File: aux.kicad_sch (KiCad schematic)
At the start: 17 parts, among them J7 USB_C_Receptacle_USB2.0_16P, J86 Conn_01x02_Pin, Q81 Si2301CDS, Q82 AO3400A, U85 DAC80508xRTE

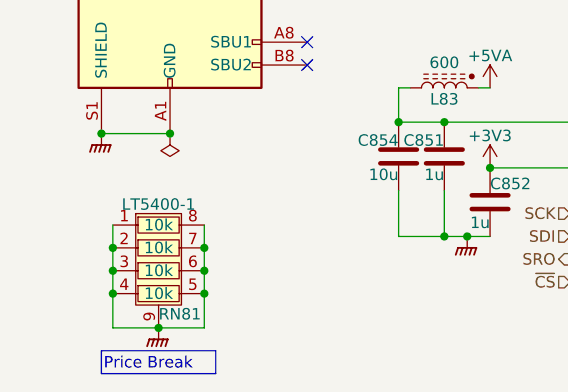
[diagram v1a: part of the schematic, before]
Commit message: Put ref filtering into the schematic.
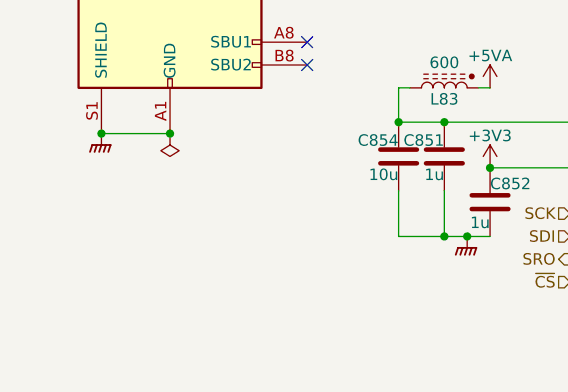
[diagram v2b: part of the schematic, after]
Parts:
- removed RN81: LT5400-1, Parts:MSOP-8-1EP_3x3mm_P0.65mm_EP1.68x1.88mm, symbol Parts:LT5400

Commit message: Progress checkin.  About to redo FDA feedback again.
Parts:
- renumbered R851 to R87, R852 to R88, R854 to R89
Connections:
- net GNDPWR: now also R89.2; no longer R89.1
- net PWR_EN: now also R89.1; no longer R89.2
- net VDAC: now reaches C851.1, C854.1, L83.2, U85.7 (VDD)
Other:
- moved on the sheet: C851, C852, C854, L83, U85

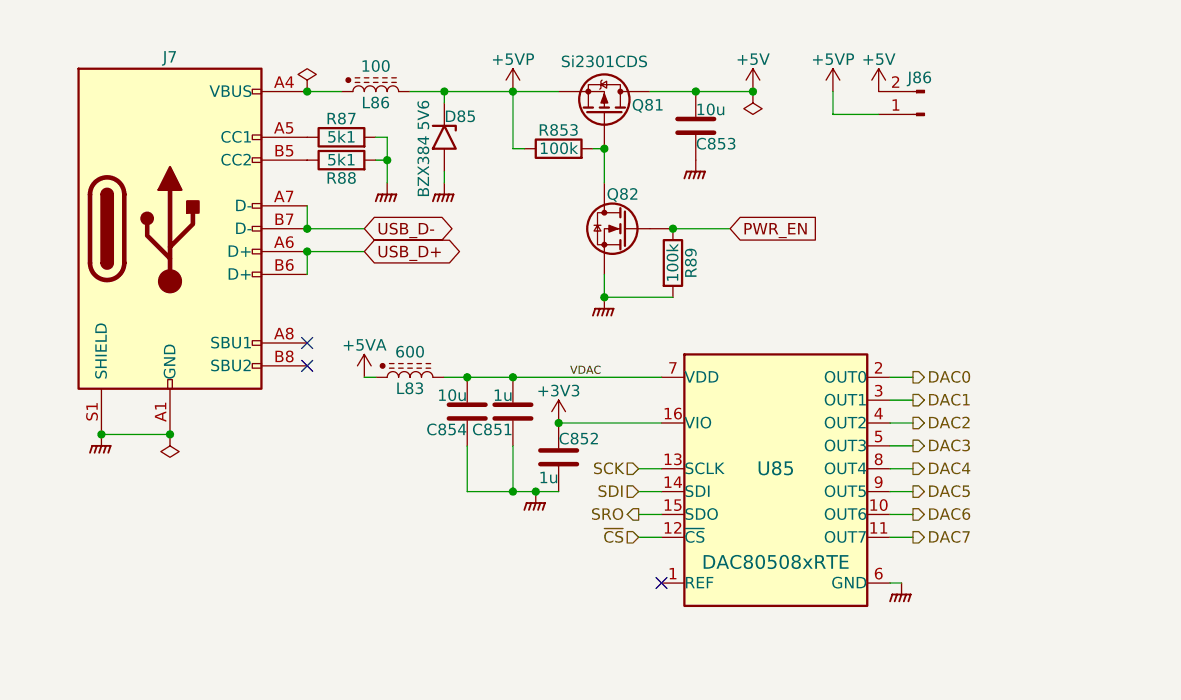
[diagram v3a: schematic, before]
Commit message: Start to place within physical board size.
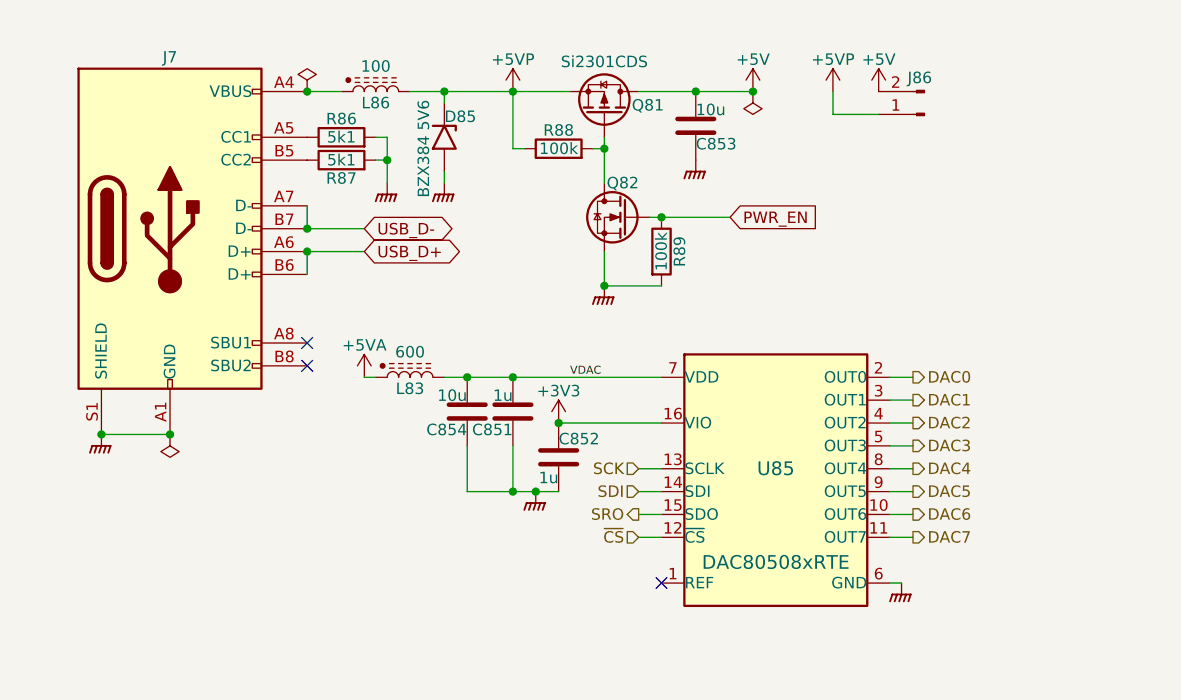
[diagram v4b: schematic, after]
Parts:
- Q81: symbol External:Si2301CDS -> Parts:Si2301CDS
- Q82: symbol Transistor_FET:AO3400A -> Parts:AO3400A; LCSC C20917 -> C15127
- renumbered R87 to R86, R88 to R87, R853 to R88
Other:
- moved on the sheet: Q81, Q82, R89
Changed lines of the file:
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@@
+	)
+	(junction
+		(at 129.54 33.02)
+		(diameter 0)
+		(color 0 0 0 0)
 	)
 	(junction
@@
 	)
 	(junction
-		(at 129.54 33.02)
-		(diameter 0)
-		(color 0 0 0 0)
-	)
-	(junction
-		(at 129.54 49.53)
+		(at 129.54 48.26)
 		(diameter 0)
 		(color 0 0 0 0)
@@
 	)
 	(junction
-		(at 137.16 41.91)
-		(diameter 0)
-		(color 0 0 0 0)
-	)
-	(junction
 		(at 119.38 71.12)
 		(diameter 0)
@@
 	)
 	(junction
+		(at 135.89 40.64)
+		(diameter 0)
+		(color 0 0 0 0)
+	)
+	(junction
 		(at 114.3 58.42)
 		(diameter 0)
@@
 	(wire
 		(pts
-			(xy 129.54 49.53) (xy 137.16 49.53)
+			(xy 129.54 48.26) (xy 135.89 48.26)
 		)
 		(stroke
@@
 	(wire
 		(pts
-			(xy 134.62 26.67) (xy 139.7 26.67)
-		)
-		(stroke
-			(width 0)
-			(type default)
-		)
-	)
-	(wire
-		(pts
 			(xy 161.29 76.2) (xy 163.83 76.2)
 		)
@@
 	(wire
 		(pts
+			(xy 129.54 31.75) (xy 129.54 33.02)
+		)
+		(stroke
+			(width 0)
+			(type default)
+		)
+	)
+	(wire
+		(pts
+			(xy 134.62 40.64) (xy 135.89 40.64)
+		)
+		(stroke
+			(width 0)
+			(type default)
+		)
+	)
+	(wire
+		(pts
 			(xy 96.52 41.91) (xy 102.87 41.91)
 		)
@@
 	(wire
 		(pts
-			(xy 129.54 46.99) (xy 129.54 49.53)
+			(xy 129.54 44.45) (xy 129.54 48.26)
 		)
 		(stroke
@@
 	(wire
 		(pts
+			(xy 133.35 26.67) (xy 139.7 26.67)
+		)
+		(stroke
+			(width 0)
+			(type default)
+		)
+	)
+	(wire
+		(pts
 			(xy 133.35 68.58) (xy 135.89 68.58)
 		)
@@
 	(wire
 		(pts
-			(xy 119.38 26.67) (xy 124.46 26.67)
+			(xy 119.38 26.67) (xy 125.73 26.67)
 		)
 		(stroke
@@
 	(wire
 		(pts
-			(xy 137.16 41.91) (xy 143.51 41.91)
+			(xy 135.89 40.64) (xy 143.51 40.64)
 		)
 		(stroke
@@
 	(global_label "PWR_EN"
 		(shape input)
-		(at 143.51 41.91 0)
+		(at 143.51 40.64 0)
 		(fields_autoplaced yes)
 		(effects
@@
 		)
 		(property "Intersheetrefs" "${INTERSHEET_REFS}"
-			(at 153.9337 41.91 0)
+			(at 153.9337 40.64 0)
 			(effects
 				(font
@@
 	)
 	(symbol
-		(lib_id "External:Si2301CDS")
+		(lib_id "Parts:Si2301CDS")
 		(at 129.54 29.21 270)
 		(mirror x)
@@
 			)
 		)
-		(property "Datasheet" "https://www.taiwansemi.com/products/datasheet/TSM2301A_C15.pdf"
+		(property "Datasheet" "~"
 			(at 125.73 24.13 0)
 			(effects
@@
 			)
 		)
-		(property "Description" "-2.8A Id, -20V Vds, P-Channel MOSFET, SOT-23"
+		(property "Description" "P-MOSFET transistor, gate/source/drain"
 			(at 129.54 29.21 0)
 			(effects
@@
 		(on_board yes)
 		(dnp no)
-		(property "Reference" "R87"
+		(property "Reference" "R86"
 			(at 100.33 29.718 90)
 			(effects
@@
 			(project "lincal"
 				(path "/b054cef4-39e3-49d8-aff0-7ba5a206c187/f6066de6-625c-453e-a76c-ce9a6a5c6264"
-					(reference "R87")
+					(reference "R86")
 					(unit 1)
 				)
@@
 		(on_board yes)
 		(dnp no)
-		(property "Reference" "R853"
+		(property "Reference" "R88"
 			(at 124.46 30.988 90)
 			(effects
@@
 			(project "lincal"
 				(path "/b054cef4-39e3-49d8-aff0-7ba5a206c187/f6066de6-625c-453e-a76c-ce9a6a5c6264"
-					(reference "R853")
+					(reference "R88")
 					(unit 1)
 				)
@@
 		(on_board yes)
 		(dnp no)
-		(property "Reference" "R88"
+		(property "Reference" "R87"
 			(at 100.33 36.322 90)
 			(effects
@@
 			(project "lincal"
 				(path "/b054cef4-39e3-49d8-aff0-7ba5a206c187/f6066de6-625c-453e-a76c-ce9a6a5c6264"
-					(reference "R88")
+					(reference "R87")
 					(unit 1)
 				)
@@
 	(symbol
 		(lib_id "power:GNDPWR")
-		(at 129.54 49.53 0)
+		(at 129.54 48.26 0)
 		(unit 1)
 		(exclude_from_sim no)
@@
 		(dnp no)
 		(property "Reference" "#PWR0104"
-			(at 129.54 55.88 0)
+			(at 129.54 54.61 0)
 			(effects
 				(font
@@
 		)
 		(property "Value" "GNDPWR"
-			(at 129.54 52.832 0)
+			(at 129.54 51.562 0)
 			(effects
 				(font
@@
 		)
 		(property "Footprint" ""
-			(at 129.54 50.8 0)
+			(at 129.54 49.53 0)
 			(effects
 				(font
@@
 		)
 		(property "Datasheet" ""
-			(at 129.54 50.8 0)
+			(at 129.54 49.53 0)
 			(effects
 				(font
@@
 		)
 		(property "Description" "Power symbol creates a global label with name \"GNDPWR\" , global ground"
-			(at 129.54 49.53 0)
+			(at 129.54 48.26 0)
 			(effects
 				(font
@@
 	)
 	(symbol
-		(lib_id "Transistor_FET:AO3400A")
-		(at 132.08 41.91 0)
+		(lib_id "Parts:AO3400A")
+		(at 132.08 40.64 0)
 		(mirror y)
 		(unit 1)
@@
 		(dnp no)
 		(property "Reference" "Q82"
-			(at 129.794 38.1 0)
+			(at 129.794 36.83 0)
 			(effects
 				(font
@@
 		)
 		(property "Value" "AO3400A"
-			(at 129.286 45.466 0)
+			(at 129.286 44.196 0)
 			(effects
 				(font
@@
 		)
 		(property "Footprint" "Parts:SOT-23"
-			(at 127 43.815 0)
+			(at 127 42.545 0)
 			(effects
 				(font
@@
 			)
 		)
-		(property "Datasheet" "http://www.aosmd.com/pdfs/datasheet/AO3400A.pdf"
-			(at 127 45.72 0)
+		(property "Datasheet" "~"
+			(at 127 44.45 0)
 			(effects
 				(font
@@
 			)
 		)
-		(property "Description" "30V Vds, 5.7A Id, N-Channel MOSFET, SOT-23"
-			(at 132.08 41.91 0)
-			(effects
-				(font
-					(size 1.27 1.27)
-				)
-				(hide yes)
-			)
-		)
-		(property "LCSC" "C20917"
-			(at 132.08 41.91 0)
+		(property "Description" "N-MOSFET transistor, gate/source/drain"
+			(at 132.08 40.64 0)
+			(effects
+				(font
+					(size 1.27 1.27)
+				)
+				(hide yes)
+			)
+		)
+		(property "LCSC" "C15127"
+			(at 132.08 40.64 0)
 			(effects
 				(font
@@
 		)
 		(property "Stock" ""
-			(at 132.08 41.91 0)
+			(at 132.08 40.64 0)
 			(effects
 				(font
@@
 	(symbol
 		(lib_id "Device:R")
-		(at 137.16 45.72 0)
+		(at 135.89 44.45 0)
 		(unit 1)
 		(exclude_from_sim no)
@@
 		(dnp no)
 		(property "Reference" "R89"
-			(at 139.192 45.72 90)
+			(at 137.922 44.45 90)
 			(effects
 				(font
@@
 		)
 		(property "Value" "100k"
-			(at 137.16 45.72 90)
+			(at 135.89 44.45 90)
 			(effects
 				(font
@@
 		)
 		(property "Footprint" "Resistor_SMD:R_0402_1005Metric"
-			(at 135.382 45.72 90)
+			(at 134.112 44.45 90)
 			(effects
 				(font
@@
 		)
 		(property "Datasheet" "~"
-			(at 137.16 45.72 0)
+			(at 135.89 44.45 0)
 			(effects
 				(font
@@
 		)
 		(property "Description" "Resistor"
-			(at 137.16 45.72 0)
+			(at 135.89 44.45 0)
 			(effects
 				(font
@@
 		)
 		(property "LCSC" "C25741"
-			(at 137.16 45.72 90)
+			(at 135.89 44.45 90)
 			(effects
 				(font
@@
 		)
 		(property "Stock" ""
-			(at 137.16 45.72 90)
-			(effects
-				(font
+			(at 135.89 44.45 90)
+			(effects
+				(font

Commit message: Nearly all routed.  Repinning FDA resistors.
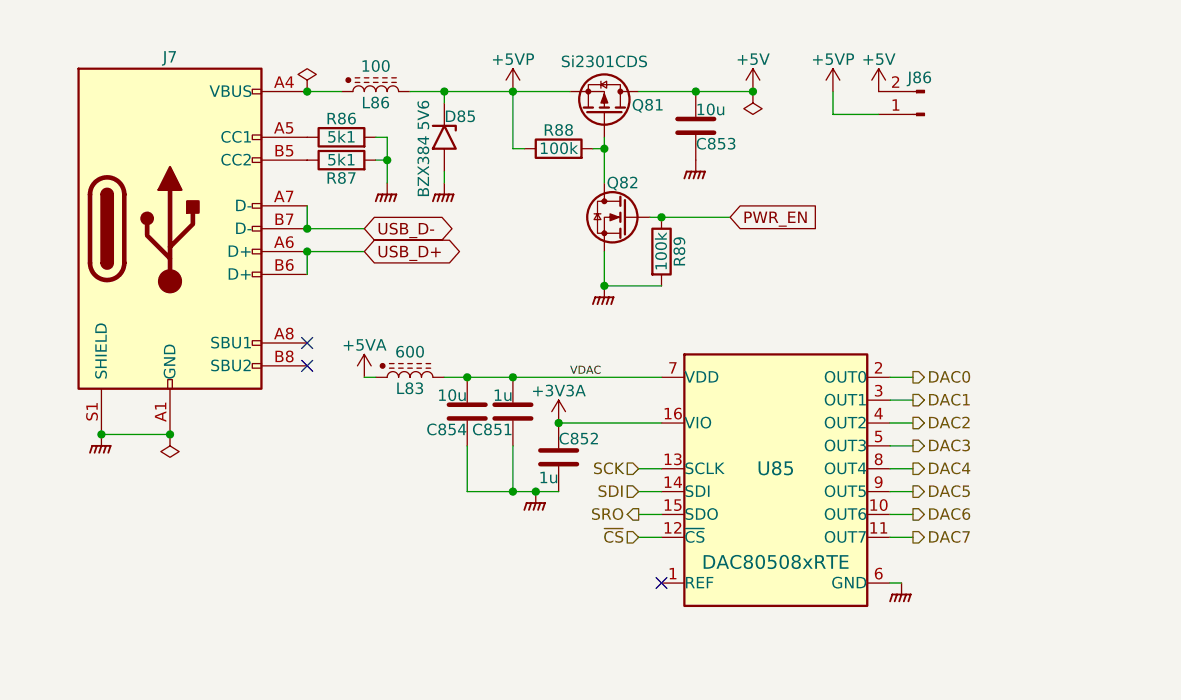
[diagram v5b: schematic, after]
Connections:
- net +3V3 renamed +3V3A
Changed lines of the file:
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@@
 	)
 	(junction
+		(at 124.46 63.5)
+		(diameter 0)
+		(color 0 0 0 0)
+	)
+	(junction
 		(at 121.92 71.12)
 		(diameter 0)
@@
 	)
 	(junction
-		(at 124.46 63.5)
-		(diameter 0)
-		(color 0 0 0 0)
-	)
-	(junction
 		(at 119.38 26.67)
 		(diameter 0)
@@
 	)
 	(symbol
-		(lib_id "power:+3V3")
-		(at 124.46 63.5 0)
-		(unit 1)
-		(exclude_from_sim no)
-		(in_bom yes)
-		(on_board yes)
-		(dnp no)
-		(property "Reference" "#PWR0164"
-			(at 124.46 67.31 0)
-			(effects
-				(font
-					(size 1.27 1.27)
-				)
-				(hide yes)
-			)
-		)
-		(property "Value" "+3V3"
-			(at 124.46 59.944 0)
-			(effects
-				(font
-					(size 1.27 1.27)
-				)
-			)
-		)
-		(property "Footprint" ""
-			(at 124.46 63.5 0)
-			(effects
-				(font
-					(size 1.27 1.27)
-				)
-				(hide yes)
-			)
-		)
-		(property "Datasheet" ""
-			(at 124.46 63.5 0)
-			(effects
-				(font
-					(size 1.27 1.27)
-				)
-				(hide yes)
-			)
-		)
-		(property "Description" "Power symbol creates a global label with name \"+3V3\""
-			(at 124.46 63.5 0)
-			(effects
-				(font
-					(size 1.27 1.27)
-				)
-				(hide yes)
-			)
-		)
-		(pin "1"
-		)
-		(instances
-			(project "lincal"
-				(path "/b054cef4-39e3-49d8-aff0-7ba5a206c187/f6066de6-625c-453e-a76c-ce9a6a5c6264"
-					(reference "#PWR0164")
-					(unit 1)
-				)
-			)
-		)
-	)
-	(symbol
 		(lib_id "Connector:USB_C_Receptacle_USB2.0_16P")
 		(at 81.28 41.91 0)
@@
 					(unit 1)
 				)
+			)
+		)
+	)
+	(symbol
+		(lib_id "Parts:+3V3A")
+		(at 124.46 63.5 0)
+		(unit 1)
+		(exclude_from_sim no)
+		(in_bom yes)
+		(on_board yes)
+		(dnp no)
+		(property "Reference" "#PWR0140"
+			(at 124.46 67.31 0)
+			(effects
+				(font
+					(size 1.27 1.27)
+				)
+				(hide yes)
+			)
+		)
+		(property "Value" "+3V3A"
+			(at 124.46 59.944 0)
+			(do_not_autoplace yes)
+			(effects
+				(font
+					(size 1.27 1.27)
+				)
+			)
+		)
+		(property "Footprint" ""
+			(at 124.46 63.5 0)
+			(effects
+				(font
+					(size 1.27 1.27)
+				)
+				(hide yes)
+			)
+		)
+		(property "Datasheet" ""
+			(at 124.46 63.5 0)
+			(effects
+				(font
+					(size 1.27 1.27)
+				)
+				(hide yes)
+			)
+		)
+		(property "Description" "Power symbol creates a global label with name {dblquote}+3V3A{dblquote}"
+			(at 124.46 63.5 0)
+			(effects
+				(font
+					(size 1.27 1.27)
+				)
+				(hide yes)
+			)
+		)
+		(pin "1"
+		)
+		(instances
+			(project "lincal"
+				(path "/b054cef4-39e3-49d8-aff0-7ba5a206c187/f6066de6-625c-453e-a76c-ce9a6a5c6264"
+					(reference "#PWR0140")
+					(unit 1)
+				)

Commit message: DRC update.  Repin ADC.  De-crack the S/H ground.
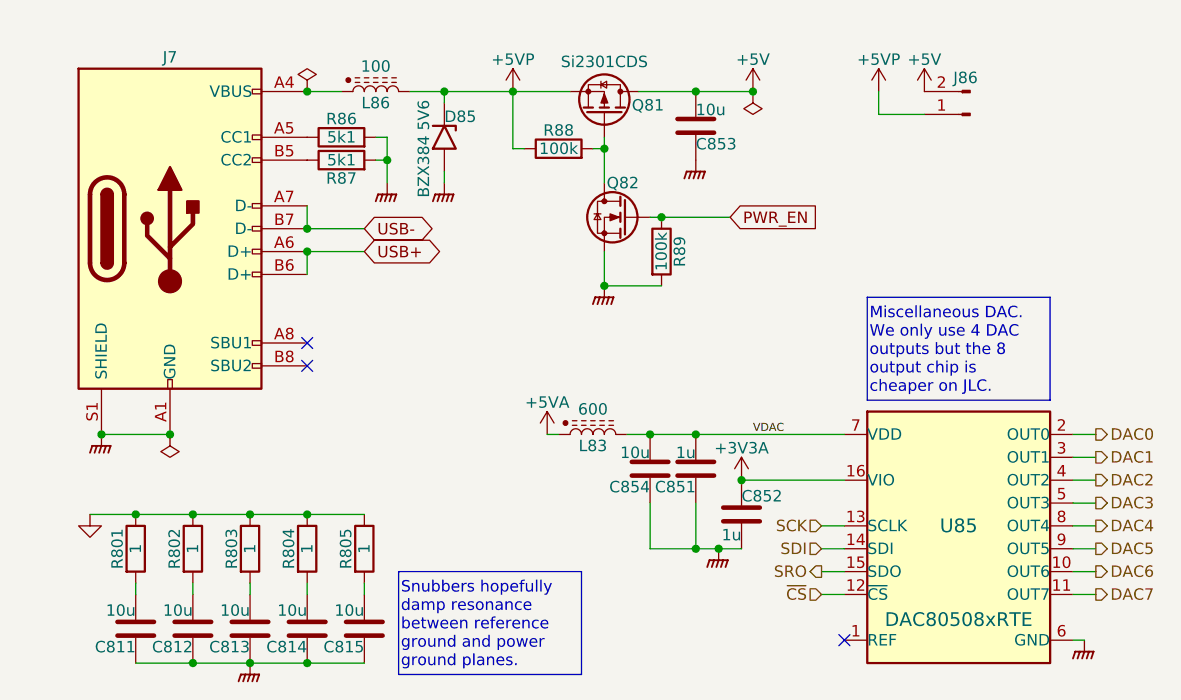
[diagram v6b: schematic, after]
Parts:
- added C811, C812, C813, C814, C815: 10u, Capacitor_SMD:C_0402_1005Metric, symbol Device:C
- added R801, R802, R803, R804, R805: 1, Resistor_SMD:R_0603_1608Metric, symbol Device:R
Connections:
- net GNDPWR: now also C811.2, C812.2, C813.2, C814.2, C815.2
- net USB_D+ renamed USB+
- net USB_D- renamed USB-
- new net: C813.1, R803.2
- new net: C815.1, R805.2
- new net: C812.1, R802.2
- new net: C814.1, R804.2
- new net: C811.1, R801.2
- new net GND: R801.1, R802.1, R803.1, R804.1, R805.1
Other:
- moved on the sheet: C851, C852, C854, J86, L83, U85

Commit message: Redo the reference ground star point.
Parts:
- removed C812, C813: 10u, Capacitor_SMD:C_0402_1005Metric, symbol Device:C
- removed R802, R803: 1, Resistor_SMD:R_0603_1608Metric, symbol Device:R

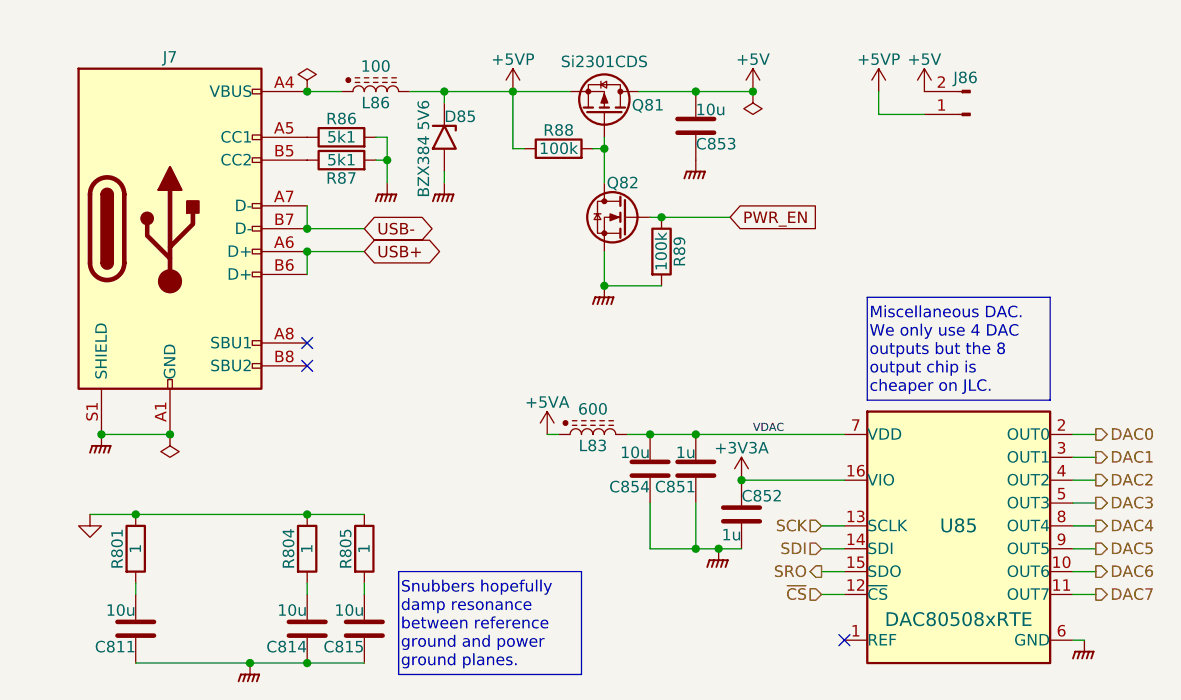
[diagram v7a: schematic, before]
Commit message: Remove placebo planes.  Tidy some analog routing.
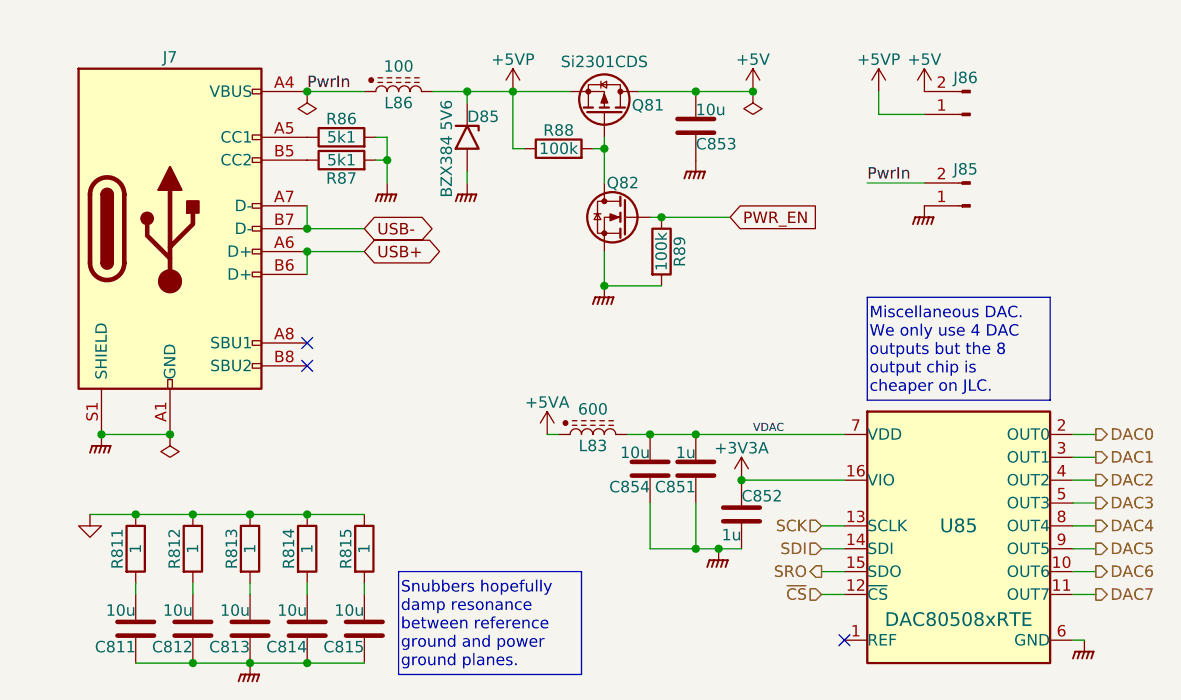
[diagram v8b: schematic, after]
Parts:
- added C812, C813: 10u, Capacitor_SMD:C_0402_1005Metric, symbol Device:C
- added J85: Conn_01x02_Pin, Parts:PinHeader_1x02_P2.54mm_Vertical, symbol Connector:Conn_01x02_Pin
- added R812, R813: 1, Resistor_SMD:R_0603_1608Metric, symbol Device:R
- renumbered R801 to R811, R804 to R814, R805 to R815
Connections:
- net GND: now also R812.1, R813.1
- net GNDPWR: now also C812.2, C813.2, J85.1 (Pin_1)
- net PwrIn: now reaches J7.A4 (VBUS), J7.A9 (VBUS), J7.B4 (VBUS), J7.B9 (VBUS), L86.1
- net PwrIn: now also J85.2 (Pin_2)
- new net: C812.1, R812.2
- new net: C813.1, R813.2
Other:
- moved on the sheet: D85, L86
